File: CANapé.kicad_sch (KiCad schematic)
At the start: 43 parts, among them J1 USB_C_Receptacle_USB2.0, J2 CAN, J3 CAN, SW1 120, SW2 120, SW3 BOOT, SW4 RST, U1 NCP1117-3.3_SOT223, U2 SN65HVD232, U3 STM32F302C6Tx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

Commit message: add pdf
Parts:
- removed H1, H2, H3, H4: m3, MountingHole:MountingHole_2.2mm_M2_DIN965_Pad, symbol Mechanical:MountingHole_Pad
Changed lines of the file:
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@@
   (junction (at 241.3 68.58) (diameter 0) (color 0 0 0 0)
   )
-  (junction (at 142.24 153.67) (diameter 0) (color 0 0 0 0)
-  )
   (junction (at 30.48 87.63) (diameter 0) (color 0 0 0 0)
   )
@@
   (junction (at 22.86 80.01) (diameter 0) (color 0 0 0 0)
   )
-  (junction (at 142.24 158.75) (diameter 0) (color 0 0 0 0)
-  )
   (junction (at 43.18 31.75) (diameter 0) (color 0 0 0 0)
   )
@@
   )
   (junction (at 247.65 76.2) (diameter 0) (color 0 0 0 0)
-  )
-  (junction (at 142.24 148.59) (diameter 0) (color 0 0 0 0)
   )
   (junction (at 74.93 19.05) (diameter 0) (color 0 0 0 0)
@@
     (stroke (width 0) (type default) (color 0 0 0 0))
   )
-  (wire (pts (xy 142.24 153.67) (xy 142.24 158.75))
-    (stroke (width 0) (type default) (color 0 0 0 0))
-  )
   (polyline (pts (xy 12.7 12.7) (xy 82.55 12.7))
     (stroke (width 0) (type default) (color 0 0 0 0))
@@
     (stroke (width 0) (type default) (color 0 0 0 0))
   )
-  (wire (pts (xy 142.24 158.75) (xy 142.24 166.37))
-    (stroke (width 0) (type default) (color 0 0 0 0))
-  )
   (wire (pts (xy 55.88 26.67) (xy 71.12 26.67))
     (stroke (width 0) (type default) (color 0 0 0 0))
   )
-  (wire (pts (xy 142.24 158.75) (xy 143.51 158.75))
-    (stroke (width 0) (type default) (color 0 0 0 0))
-  )
   (wire (pts (xy 152.4 116.84) (xy 152.4 119.38))
     (stroke (width 0) (type default) (color 0 0 0 0))
@@
     (stroke (width 0) (type default) (color 0 0 0 0))
   )
-  (wire (pts (xy 142.24 148.59) (xy 142.24 153.67))
-    (stroke (width 0) (type default) (color 0 0 0 0))
-  )
   (wire (pts (xy 175.26 95.25) (xy 165.1 95.25))
     (stroke (width 0) (type default) (color 0 0 0 0))
@@
     (stroke (width 0) (type default) (color 0 0 0 0))
   )
-  (wire (pts (xy 142.24 142.24) (xy 142.24 148.59))
-    (stroke (width 0) (type default) (color 0 0 0 0))
-  )
   (wire (pts (xy 247.65 76.2) (xy 254 76.2))
     (stroke (width 0) (type default) (color 0 0 0 0))
@@
     (stroke (width 0) (type default) (color 0 0 0 0))
   )
-  (wire (pts (xy 142.24 153.67) (xy 143.51 153.67))
-    (stroke (width 0) (type default) (color 0 0 0 0))
-  )
   (wire (pts (xy 215.9 64.77) (xy 215.9 67.31))
     (stroke (width 0) (type default) (color 0 0 0 0))
@@
     (stroke (width 0) (type default) (color 0 0 0 0))
   )
-  (wire (pts (xy 142.24 148.59) (xy 143.51 148.59))
-    (stroke (width 0) (type default) (color 0 0 0 0))
-  )
   (wire (pts (xy 226.06 125.73) (xy 231.14 125.73))
     (stroke (width 0) (type default) (color 0 0 0 0))
@@
   )
   (wire (pts (xy 48.26 57.15) (xy 54.61 57.15))
-    (stroke (width 0) (type default) (color 0 0 0 0))
-  )
-  (wire (pts (xy 143.51 142.24) (xy 142.24 142.24))
     (stroke (width 0) (type default) (color 0 0 0 0))
   )
@@
     (pin "9")
   )
-  (symbol (lib_id "power:GND") (at 142.24 166.37 0) (unit 1)
-    (in_bom yes) (on_board yes)
-    (property "Reference" "#PWR027" (id 0) (at 142.24 172.72 0)
-      (effects (font (size 1.27 1.27)) hide)
-    )
-    (property "Value" "GND" (id 1) (at 142.367 170.7642 0))
-    (property "Footprint" "" (id 2) (at 142.24 166.37 0)
-      (effects (font (size 1.27 1.27)) hide)
-    )
-    (property "Datasheet" "" (id 3) (at 142.24 166.37 0)
-      (effects (font (size 1.27 1.27)) hide)
-    )
-    (pin "1")
-  )
   (symbol (lib_id "power:GND") (at 48.26 57.15 0) (unit 1)
     (in_bom yes) (on_board yes)
@@
     (pin "2")
   )
-  (symbol (lib_id "Mechanical:MountingHole_Pad") (at 146.05 148.59 270) (unit 1)
-    (in_bom yes) (on_board yes) (fields_autoplaced)
-    (property "Reference" "H2" (id 0) (at 149.86 147.7553 90)
-      (effects (font (size 1.27 1.27)) (justify left))
-    )
-    (property "Value" "m3" (id 1) (at 149.86 150.2922 90)
-      (effects (font (size 1.27 1.27)) (justify left))
-    )
-    (property "Footprint" "MountingHole:MountingHole_2.2mm_M2_DIN965_Pad" (id 2) (at 146.05 148.59 0)
-      (effects (font (size 1.27 1.27)) hide)
-    )
-    (property "Datasheet" "~" (id 3) (at 146.05 148.59 0)
-      (effects (font (size 1.27 1.27)) hide)
-    )
-    (pin "1")
-  )
   (symbol (lib_id "power:+3.3V") (at 241.3 123.19 0) (unit 1)
     (in_bom yes) (on_board yes)
@@
     (pin "1")
     (pin "2")
-  )
-  (symbol (lib_id "Mechanical:MountingHole_Pad") (at 146.05 158.75 270) (unit 1)
-    (in_bom yes) (on_board yes) (fields_autoplaced)
-    (property "Reference" "H4" (id 0) (at 149.86 157.9153 90)
-      (effects (font (size 1.27 1.27)) (justify left))
-    )
-    (property "Value" "m3" (id 1) (at 149.86 160.4522 90)
-      (effects (font (size 1.27 1.27)) (justify left))
-    )
-    (property "Footprint" "MountingHole:MountingHole_2.2mm_M2_DIN965_Pad" (id 2) (at 146.05 158.75 0)
-      (effects (font (size 1.27 1.27)) hide)
-    )
-    (property "Datasheet" "~" (id 3) (at 146.05 158.75 0)
-      (effects (font (size 1.27 1.27)) hide)
-    )
-    (pin "1")
   )
   (symbol (lib_id "Device:R") (at 52.07 26.67 90) (unit 1)
@@
     (pin "2")
   )
-  (symbol (lib_id "Mechanical:MountingHole_Pad") (at 146.05 142.24 270) (unit 1)
-    (in_bom yes) (on_board yes) (fields_autoplaced)
-    (property "Reference" "H1" (id 0) (at 149.86 141.4053 90)
-      (effects (font (size 1.27 1.27)) (justify left))
-    )
-    (property "Value" "m3" (id 1) (at 149.86 143.9422 90)
-      (effects (font (size 1.27 1.27)) (justify left))
-    )
-    (property "Footprint" "MountingHole:MountingHole_2.2mm_M2_DIN965_Pad" (id 2) (at 146.05 142.24 0)
-      (effects (font (size 1.27 1.27)) hide)
-    )
-    (property "Datasheet" "~" (id 3) (at 146.05 142.24 0)
-      (effects (font (size 1.27 1.27)) hide)
-    )
-    (pin "1")
-  )
   (symbol (lib_id "Device:C") (at 38.1 83.82 180) (unit 1)
     (in_bom yes) (on_board yes)
@@
     (pin "1")
     (pin "2")
-  )
-  (symbol (lib_id "Mechanical:MountingHole_Pad") (at 146.05 153.67 270) (unit 1)
-    (in_bom yes) (on_board yes) (fields_autoplaced)
-    (property "Reference" "H3" (id 0) (at 149.86 152.8353 90)
-      (effects (font (size 1.27 1.27)) (justify left))
-    )
-    (property "Value" "m3" (id 1) (at 149.86 155.3722 90)
-      (effects (font (size 1.27 1.27)) (justify left))
-    )
-    (property "Footprint" "MountingHole:MountingHole_2.2mm_M2_DIN965_Pad" (id 2) (at 146.05 153.67 0)
-      (effects (font (size 1.27 1.27)) hide)
-    )
-    (property "Datasheet" "~" (id 3) (at 146.05 153.67 0)
-      (effects (font (size 1.27 1.27)) hide)
-    )
-    (pin "1")
   )
   (symbol (lib_id "power:GND") (at 35.56 121.92 0) (unit 1)
@@
       (reference "#PWR026") (unit 1) (value "GND") (footprint "")
     )
-    (path "/6423d55d-13b8-4401-9c5a-99a6ed9c42e7"
-      (reference "#PWR027") (unit 1) (value "GND") (footprint "")
-    )
     (path "/b51f6278-a4d5-4d0b-8bc2-4a75331e40d5"
       (reference "C1") (unit 1) (value "10u") (footprint "Capacitor_SMD:C_0805_2012Metric_Pad1.18x1.45mm_HandSolder")
@@
       (reference "D5") (unit 1) (value "LED_DEBUG") (footprint "LED_SMD:LED_0805_2012Metric_Pad1.15x1.40mm_HandSolder")
     )
-    (path "/c1212456-d2b9-440c-9946-508c16588497"
-      (reference "H1") (unit 1) (value "m3") (footprint "MountingHole:MountingHole_2.2mm_M2_DIN965_Pad")
-    )
-    (path "/9f565822-f307-4eb0-afe4-4ee11e8bf37e"
-      (reference "H2") (unit 1) (value "m3") (footprint "MountingHole:MountingHole_2.2mm_M2_DIN965_Pad")
-    )
-    (path "/deefd0d1-7017-498b-9ea5-cccdfa6cc861"
-      (reference "H3") (unit 1) (value "m3") (footprint "MountingHole:MountingHole_2.2mm_M2_DIN965_Pad")
-    )
-    (path "/a37ea250-0edd-4e02-a2b9-f8251c32c3b0"
-      (reference "H4") (unit 1) (value "m3") (footprint "MountingHole:MountingHole_2.2mm_M2_DIN965_Pad")
-    )
     (path "/38427f64-7323-4d4d-b3ca-d2531d728e2a"

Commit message: update
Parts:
- removed J2: CAN, AREA_lib_Connector:690367290476, symbol Connector:Conn_01x04_Female
- removed J3: CAN, Connector_PinHeader_2.54mm:PinHeader_1x04_P2.54mm_Vertical, symbol Connector:Conn_01x04_Female
- removed SW1: 120, Button_Switch_THT:SW_Push_1P2T_Vertical_E-Switch_800UDP8P1A1M6, symbol Switch:SW_Push_SPDT
- added J2: DB9_Male_MountingHoles, Connector_Dsub:DSUB-9_Male_Horizontal_P2.77x2.84mm_EdgePinOffset7.70mm_Housed_MountingHolesOffset9.12mm, symbol Connector:DB9_Male_MountingHoles
- C1, C10, C11, C12, C13, C14, C2, C3, C4, C5, C6, C7, C8, C9: footprint Capacitor_SMD:C_0805_2012Metric_Pad1.18x1.45mm_HandSolder -> Capacitor_SMD:C_0805_2012Metric
- D1, D2, D4, D5: footprint LED_SMD:LED_0805_2012Metric_Pad1.15x1.40mm_HandSolder -> LED_SMD:LED_0805_2012Metric
- R1, R2, R3, R4, R5, R6, R7, R8, R9: footprint Resistor_SMD:R_0805_2012Metric_Pad1.20x1.40mm_HandSolder -> Resistor_SMD:R_0805_2012Metric
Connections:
- net CANH: now also J2.7
- net CANL: now also J2.2
- net GND: now also J2.0 (PAD), J2.3, J2.5, J2.6
- net RX: no longer names the net of U3.31 (PA10)
- net TX: no longer names the net of U3.30 (PA9)
- no-connect marks 9 -> 7
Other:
- moved on the sheet: C11

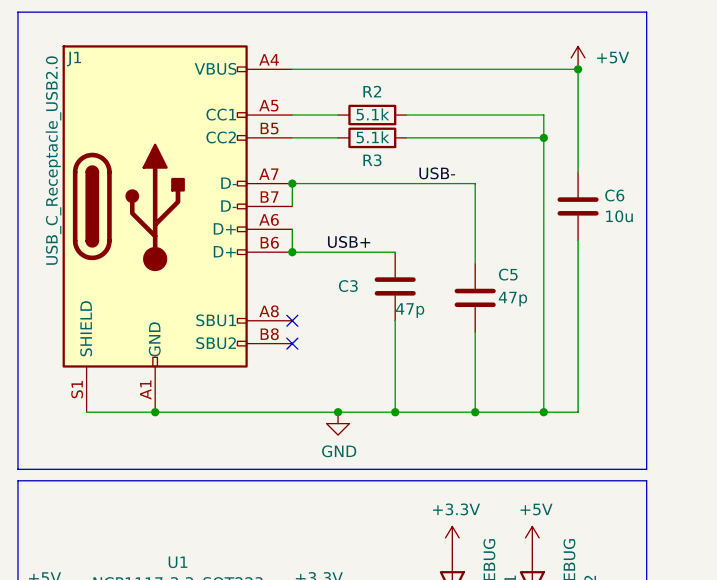
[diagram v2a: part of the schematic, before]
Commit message: v2 with db9 connector
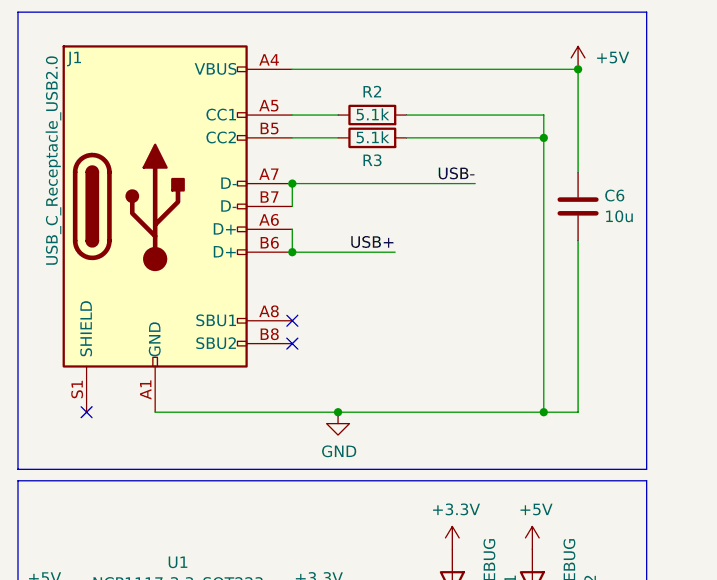
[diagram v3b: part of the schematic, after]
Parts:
- removed C3, C5: 47p, Capacitor_SMD:C_0805_2012Metric, symbol Device:C
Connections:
- net GND: no longer J1.S1 (SHIELD)
- no-connect marks 7 -> 8
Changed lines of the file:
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@@
 (kicad_sch (version 20211123) (generator eeschema)
   (paper "A4")
-  (junction (at 54.61 57.15) (diameter 0) (color 0 0 0 0)
-  )
   (junction (at 260.35 76.2) (diameter 0) (color 0 0 0 0)
   )
@@
   (junction (at 254 68.58) (diameter 0) (color 0 0 0 0)
   )
-  (junction (at 63.5 57.15) (diameter 0) (color 0 0 0 0)
-  )
   (junction (at 254 76.2) (diameter 0) (color 0 0 0 0)
   )
@@
   )
   (junction (at 210.82 146.05) (diameter 0) (color 0 0 0 0)
-  )
-  (junction (at 27.94 57.15) (diameter 0) (color 0 0 0 0)
   )
   (junction (at 241.3 76.2) (diameter 0) (color 0 0 0 0)
@@
   (no_connect (at 43.18 46.99))
   (no_connect (at 43.18 49.53))
+  (no_connect (at 20.32 57.15))
   (wire (pts (xy 193.04 77.47) (xy 189.23 77.47))
     (stroke (width 0) (type default) (color 0 0 0 0))
@@
     (stroke (width 0) (type default) (color 0 0 0 0))
   )
-  (wire (pts (xy 63.5 48.26) (xy 63.5 57.15))
-    (stroke (width 0) (type default) (color 0 0 0 0))
-  )
   (wire (pts (xy 189.23 99.06) (xy 189.23 85.09))
     (stroke (width 0) (type default) (color 0 0 0 0))
@@
     (stroke (width 0) (type default) (color 0 0 0 0))
   )
-  (wire (pts (xy 63.5 31.75) (xy 63.5 40.64))
-    (stroke (width 0) (type default) (color 0 0 0 0))
-  )
   (wire (pts (xy 71.12 26.67) (xy 71.12 57.15))
     (stroke (width 0) (type default) (color 0 0 0 0))
@@
     (stroke (width 0) (type default) (color 0 0 0 0))
   )
-  (wire (pts (xy 54.61 57.15) (xy 63.5 57.15))
+  (wire (pts (xy 48.26 57.15) (xy 71.12 57.15))
     (stroke (width 0) (type default) (color 0 0 0 0))
   )
@@
     (stroke (width 0) (type default) (color 0 0 0 0))
   )
-  (wire (pts (xy 63.5 57.15) (xy 71.12 57.15))
-    (stroke (width 0) (type default) (color 0 0 0 0))
-  )
   (wire (pts (xy 237.49 76.2) (xy 241.3 76.2))
     (stroke (width 0) (type default) (color 0 0 0 0))
@@
     (stroke (width 0) (type default) (color 0 0 0 0))
   )
-  (wire (pts (xy 20.32 57.15) (xy 27.94 57.15))
-    (stroke (width 0) (type default) (color 0 0 0 0))
-  )
   (wire (pts (xy 74.93 57.15) (xy 74.93 38.1))
     (stroke (width 0) (type default) (color 0 0 0 0))
@@
     (stroke (width 0) (type default) (color 0 0 0 0))
   )
-  (wire (pts (xy 48.26 57.15) (xy 54.61 57.15))
-    (stroke (width 0) (type default) (color 0 0 0 0))
-  )
   (wire (pts (xy 55.88 104.14) (xy 55.88 109.22))
     (stroke (width 0) (type default) (color 0 0 0 0))
@@
   )
   (wire (pts (xy 43.18 26.67) (xy 48.26 26.67))
-    (stroke (width 0) (type default) (color 0 0 0 0))
-  )
-  (wire (pts (xy 54.61 46.99) (xy 54.61 57.15))
     (stroke (width 0) (type default) (color 0 0 0 0))
   )
@@
     (effects (font (size 1.27 1.27)) (justify left bottom))
   )
-  (label "USB+" (at 46.99 39.37 0)
-    (effects (font (size 1.27 1.27)) (justify left bottom))
-  )
-  (label "USB-" (at 57.15 31.75 0)
-    (effects (font (size 1.27 1.27)) (justify left bottom))
+  (label "USB+" (at 54.61 39.37 180)
+    (effects (font (size 1.27 1.27)) (justify right bottom))
+  )
+  (label "USB-" (at 63.5 31.75 180)
+    (effects (font (size 1.27 1.27)) (justify right bottom))
   )
   (label "RST" (at 257.81 49.53 0)
@@
     )
     (pin "1")
-  )
-  (symbol (lib_id "Device:C") (at 63.5 44.45 0) (unit 1)
-    (in_bom yes) (on_board yes)
-    (property "Reference" "C5" (id 0) (at 66.04 41.91 0)
-      (effects (font (size 1.27 1.27)) (justify left))
-    )
-    (property "Value" "47p" (id 1) (at 66.04 44.45 0)
-      (effects (font (size 1.27 1.27)) (justify left))
-    )
-    (property "Footprint" "Capacitor_SMD:C_0805_2012Metric" (id 2) (at 64.4652 48.26 0)
-      (effects (font (size 1.27 1.27)) hide)
-    )
-    (property "Datasheet" "~" (id 3) (at 63.5 44.45 0)
-      (effects (font (size 1.27 1.27)) hide)
-    )
-    (pin "1")
-    (pin "2")
   )
   (symbol (lib_id "power:GND") (at 152.4 119.38 0) (unit 1)
@@
     (pin "1")
   )
-  (symbol (lib_id "Device:C") (at 54.61 43.18 0) (unit 1)
-    (in_bom yes) (on_board yes)
-    (property "Reference" "C3" (id 0) (at 48.26 43.18 0)
-      (effects (font (size 1.27 1.27)) (justify left))
-    )
-    (property "Value" "47p" (id 1) (at 54.61 45.72 0)
-      (effects (font (size 1.27 1.27)) (justify left))
-    )
-    (property "Footprint" "Capacitor_SMD:C_0805_2012Metric" (id 2) (at 55.5752 46.99 0)
-      (effects (font (size 1.27 1.27)) hide)
-    )
-    (property "Datasheet" "~" (id 3) (at 54.61 43.18 0)
-      (effects (font (size 1.27 1.27)) hide)
-    )
-    (pin "1")
-    (pin "2")
-  )
   (symbol (lib_id "power:GND") (at 35.56 121.92 0) (unit 1)
     (in_bom yes) (on_board yes)
@@
       (reference "C2") (unit 1) (value "10u") (footprint "Capacitor_SMD:C_0805_2012Metric")
     )
-    (path "/dd0b0fbb-8b62-4f2c-abcd-2ccc1a628368"
-      (reference "C3") (unit 1) (value "47p") (footprint "Capacitor_SMD:C_0805_2012Metric")
-    )
     (path "/04721b2a-b8fe-4628-b3cc-831c2dbc8b4f"
       (reference "C4") (unit 1) (value "100nF") (footprint "Capacitor_SMD:C_0805_2012Metric")
     )
-    (path "/4106bf28-b2bb-4ec5-83d6-380ec5f54bf3"
-      (reference "C5") (unit 1) (value "47p") (footprint "Capacitor_SMD:C_0805_2012Metric")
-    )
     (path "/719abcb6-7628-4b94-a978-acb5e0f7b473"
